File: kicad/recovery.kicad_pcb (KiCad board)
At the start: 2 copper layers, 84.1 x 61.7 mm, 40 parts, among them J1 Bus_PCI_Express_x1, J4 Conn_01x02, J6 USB_C_Receptacle_USB2.0_16P, U2 RP2040, U4 W25Q128JVP, U9 MCP25625T-E/ML, X1 ABM8-272-T3, Y2 X322516MLB4SI

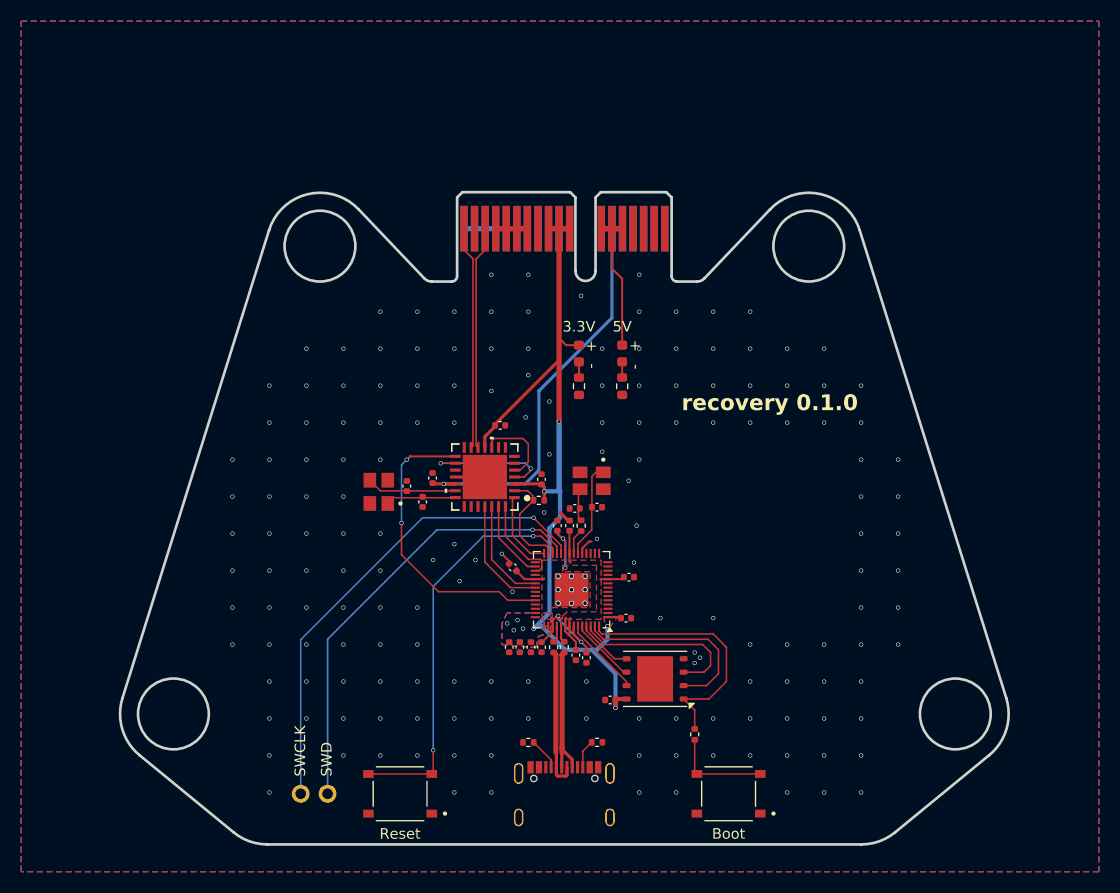
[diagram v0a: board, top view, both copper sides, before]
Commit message: add wago connectors, update components with chips from new library
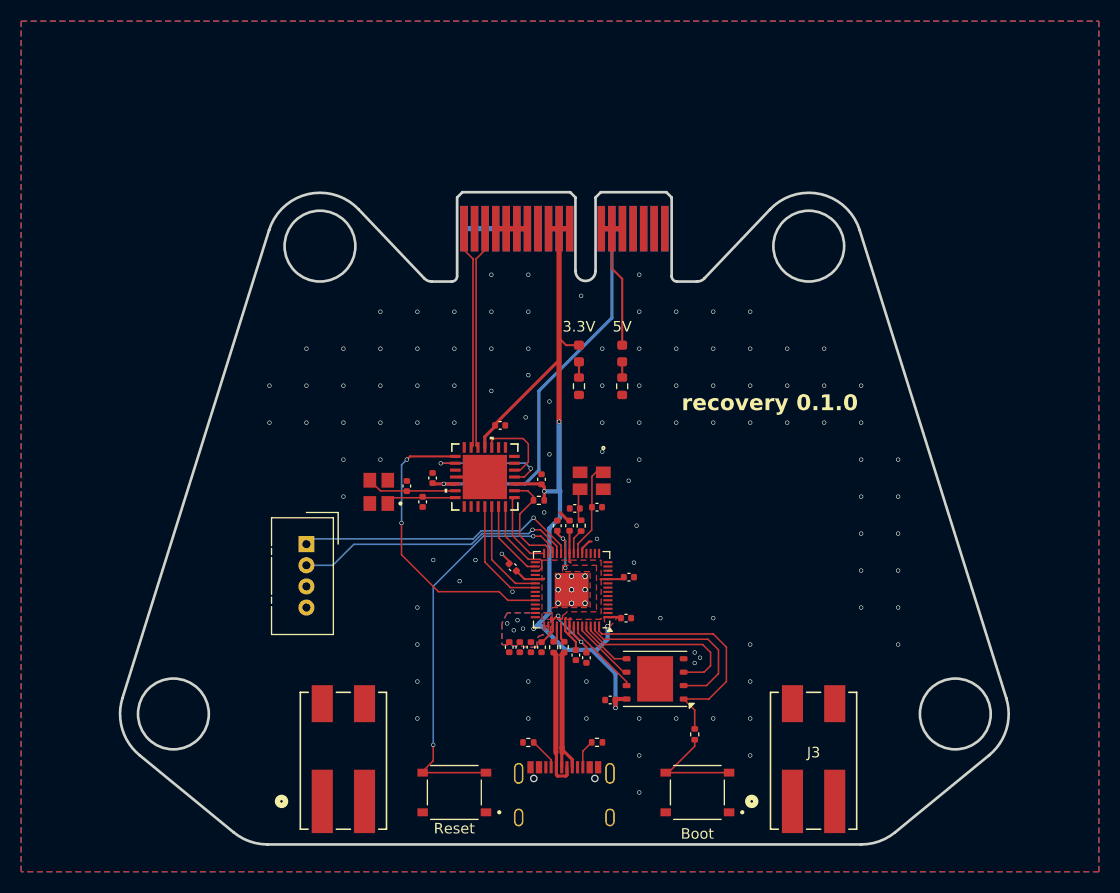
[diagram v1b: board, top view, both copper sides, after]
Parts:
- added J2: wago 2060-452/998-404, recovery:wago-2060-452_998-404, F.Cu at (125.5, 114.5)
- added J3: wago 2060-452/998-404, recovery:wago-2060-452_998-404, F.Cu at (170.0, 114.5)
- J4: value Conn_01x02 -> Conn_01x04; footprint Connector_PinHeader_2.54mm:PinHeader_1x02_P2.54mm_Vertical -> Connector:NS-Tech_Grove_1x04_P2mm_Vertical
- R1, R2: value 150 -> 1k
- S1, S2: footprint TS-1187A-B-A-B:SW_TS-1187A-B-A-B -> 4in-kicad-library:TS-1187A-B-A-B
- U9: footprint MCP25625T_E_ML:QFN28_6X6MC_MCH -> 4in-kicad-library:QFN28_6X6MC_MCH
- X1: value ABM8-272-T3 -> RP2040 Crystal; footprint ABM8-272-T3:ABM8-272-T3_ABR -> 4in-kicad-library:ABM8-272-T3_ABR
- Y2: footprint X322516MLB4SI:OSC_X322516MLB4SI -> 4in-kicad-library:X322516MLB4SI
- moved J4 23.6 mm to (122.0, 94.0), turned to 0 degrees
- moved S2 5.14 mm to (136.0, 117.5)
- moved S1 2.96 mm to (159.0, 117.5)
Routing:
- net /SWCLK: track 45.9 -> 27.0 mm
- net /SWD: track 41.8 -> 26.3 mm
- net /~{USB_BOOT_S}: track 9.32 -> 10.4 mm
- net GND: vias 183 -> 117
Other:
- board text removed: "SWCLK"
- board text removed: "SWD"
